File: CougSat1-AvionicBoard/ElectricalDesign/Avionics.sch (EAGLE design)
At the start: 195 parts, among them J11 -Y, J12 +Z, J13 +X, J14 -Z, J15 +Y, J3 SWD, J4 CougSat Card, J5 -X, J8 SWD, J9 SWD, U1 STM32L476RGT, U10 BNO055, U11 128KB, U12 TXS0102DQM, U13 TXS0102DQM, U14 AD8515, U15 BNO055, U16 BNO055, U17 TXS0102DQM, U18 TXS0102DQM, U19 INA199C1, U2 STM32L476RGT, U20 INA199C1, U21 INA199C1, U24 AD8515, U25 AD7291, U26 AD7291, U29 AD8515, U3 STM32L476RGT, U4 128KB, U5 DRV8837, U6 DRV8837, U7 DRV8837, U8 AD7291, U9 Venus838FLPx-L, Y1 16MHz ±10ppm, Y10 16MHz ±10ppm, Y2 32.768kHz ±10ppm, Y3 16MHz ±10ppm, Y4 32.768kHz ±10ppm, Y6 32.768kHz ±10ppm, Y7 32.768kHz ±10ppm, Y8 32.768kHz ±10ppm, Y9 32.768kHz ±10ppm

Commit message: Resolved Errors
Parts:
- J10: value (none) -> iFJR SD1
- J16: value (none) -> IFJR SD0
- J2: value (none) -> IHU SD1
- J6: value (none) -> IHU SD0
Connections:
- new net RFGND: AE1.SHIELD, R4.1, U9BASE.RFGND
- net 3.3V_0: now also C25.1, C26.1
- net AGND: no longer AE1.SHIELD, R4.1, U9BASE.RFGND
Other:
- note removed: "3D3>"
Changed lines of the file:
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@@
 <part name="SUPPLY3" library="CougsInSpace-PowerSymbols" deviceset="AGND" device=""/>
 <part name="SUPPLY4" library="CougsInSpace-PowerSymbols" deviceset="CHASSIS" device=""/>
-<part name="SUPPLY5" library="CougsInSpace-PowerSymbols" deviceset="RFGND" device=""/>
 <part name="SUPPLY6" library="CougsInSpace-PowerSymbols" deviceset="DGND" device=""/>
 <part name="SUPPLY7" library="CougsInSpace-PowerSymbols" deviceset="DGND" device=""/>
@@
 <part name="R12" library="CougsInSpace-Resistors" deviceset="RES-V" device="-1608" technology="-33K" value="33kΩ 1%"/>
 <part name="SUPPLY56" library="CougsInSpace-PowerSymbols" deviceset="DGND" device=""/>
-<part name="SUPPLY57" library="CougsInSpace-PowerSymbols" deviceset="RFGND" device=""/>
 <part name="R13" library="CougsInSpace-Resistors" deviceset="RES-H" device="-1608" technology="-1K" value="1kΩ 0.1%"/>
 <part name="DS1" library="CougsInSpace-LEDs" deviceset="LED-V" device="-1608" technology="-GRN" value="Green"/>
@@
 <part name="OFFSHEET167" library="CougsInSpace-Aesthetics" deviceset="OFF_SHEET-OUT" device=""/>
 <part name="OFFSHEET168" library="CougsInSpace-Aesthetics" deviceset="OFF_SHEET-IN" device=""/>
-<part name="J10" library="CougsInSpace-Connectors" deviceset="µSD-SW" device="-PUSH-PUSH"/>
-<part name="J16" library="CougsInSpace-Connectors" deviceset="µSD-SW" device="-PUSH-PUSH"/>
+<part name="J10" library="CougsInSpace-Connectors" deviceset="µSD-SW" device="-PUSH-PUSH" value="iFJR SD1"/>
+<part name="J16" library="CougsInSpace-Connectors" deviceset="µSD-SW" device="-PUSH-PUSH" value="IFJR SD0"/>
 <part name="SUPPLY115" library="CougsInSpace-PowerSymbols" deviceset="DGND" device=""/>
 <part name="SUPPLY116" library="CougsInSpace-PowerSymbols" deviceset="DGND" device=""/>
@@
 <part name="C33" library="CougsInSpace-Capacitors" deviceset="CAP-V" device="-3216" technology="-100NF" value="100nF 10%"/>
 <part name="C35" library="CougsInSpace-Capacitors" deviceset="CAP-V" device="-1608" technology="-6.8NF" value="6.8nF 5%"/>
-<part name="J2" library="CougsInSpace-Connectors" deviceset="µSD-SW" device="-PUSH-PUSH"/>
-<part name="J6" library="CougsInSpace-Connectors" deviceset="µSD-SW" device="-PUSH-PUSH"/>
+<part name="J2" library="CougsInSpace-Connectors" deviceset="µSD-SW" device="-PUSH-PUSH" value="IHU SD1"/>
+<part name="J6" library="CougsInSpace-Connectors" deviceset="µSD-SW" device="-PUSH-PUSH" value="IHU SD0"/>
 <part name="SUPPLY75" library="CougsInSpace-PowerSymbols" deviceset="DGND" device=""/>
 <part name="SUPPLY76" library="CougsInSpace-PowerSymbols" deviceset="DGND" device=""/>
@@
 <part name="SUPPLY79" library="CougsInSpace-PowerSymbols" deviceset="3.3V-0" device=""/>
 <part name="SUPPLY81" library="CougsInSpace-PowerSymbols" deviceset="3.3V-0" device=""/>
+<part name="SUPPLY91" library="CougsInSpace-PowerSymbols" deviceset="3.3V-0" device=""/>
+<part name="SUPPLY92" library="CougsInSpace-PowerSymbols" deviceset="3.3V-0" device=""/>
+<part name="SUPPLY5" library="CougsInSpace-PowerSymbols" deviceset="RFGND" device=""/>
+<part name="SUPPLY57" library="CougsInSpace-PowerSymbols" deviceset="RFGND" device=""/>
 </parts>
 <sheets>
@@
 <instance part="SUPPLY3" gate="G$1" x="30.48" y="10.16" smashed="yes"/>
 <instance part="SUPPLY4" gate="G$1" x="45.72" y="10.16" smashed="yes"/>
-<instance part="SUPPLY5" gate="G$1" x="60.96" y="10.16" smashed="yes"/>
 <instance part="DIA23" gate="G$1" x="172.72" y="121.92" smashed="yes"/>
 <instance part="DIA24" gate="G$1" x="205.74" y="121.92" smashed="yes"/>
+<instance part="SUPPLY5" gate="G$1" x="60.96" y="10.16" smashed="yes"/>
 </instances>
 <busses>
@@
 <wire x1="30.48" y1="15.24" x2="30.48" y2="12.7" width="0.1524" layer="91"/>
 </segment>
-<segment>
-<pinref part="R4" gate="G$1" pin="1"/>
-<pinref part="SUPPLY5" gate="G$1" pin="RFGND"/>
-<wire x1="60.96" y1="15.24" x2="60.96" y2="12.7" width="0.1524" layer="91"/>
-</segment>
 </net>
 <net name="CHASSIS" class="0">
@@
 </segment>
 </net>
+<net name="RFGND" class="0">
+<segment>
+<pinref part="R4" gate="G$1" pin="1"/>
+<pinref part="SUPPLY5" gate="G$1" pin="RFGND"/>
+<wire x1="60.96" y1="15.24" x2="60.96" y2="12.7" width="0.1524" layer="91"/>
+</segment>
+</net>
 </nets>
 </sheet>
@@
 <text x="200.66" y="127" size="1.27" layer="97" align="center-left"> &lt;9B6</text>
 <text x="48.26" y="124.46" size="1.27" layer="97" align="center-left">   3D5&gt;</text>
-<text x="144.78" y="127" size="1.27" layer="97" align="center-left">   3D3&gt;</text>
 <text x="200.66" y="40.64" size="1.27" layer="97" align="center-right">3B2&gt; </text>
 <wire x1="91.44" y1="60.96" x2="91.44" y2="33.02" width="0.1524" layer="97" style="shortdash"/>
@@
 </instance>
 <instance part="SUPPLY56" gate="1" x="73.66" y="86.36" smashed="yes"/>
-<instance part="SUPPLY57" gate="G$1" x="114.3" y="114.3" smashed="yes"/>
 <instance part="R13" gate="G$1" x="132.08" y="99.06" smashed="yes">
 <attribute name="NAME" x="130.81" y="101.092" size="1.27" layer="95" align="center"/>
@@
 <attribute name="VALUE" x="60.96" y="77.216" size="1.27" layer="96" align="center"/>
 </instance>
+<instance part="SUPPLY57" gate="G$1" x="116.84" y="114.3" smashed="yes"/>
 </instances>
 <busses>
@@
 <net name="AGND" class="0">
 <segment>
-<pinref part="U9" gate="BASE" pin="RFGND"/>
-<wire x1="101.6" y1="116.84" x2="114.3" y2="116.84" width="0.1524" layer="91"/>
-<pinref part="SUPPLY57" gate="G$1" pin="RFGND"/>
-<wire x1="114.3" y1="116.84" x2="124.46" y2="116.84" width="0.1524" layer="91"/>
-<junction x="114.3" y="116.84"/>
-<pinref part="AE1" gate="G$1" pin="SHIELD"/>
-</segment>
-<segment>
 <pinref part="RT1" gate="G$1" pin="1"/>
 <pinref part="SUPPLY97" gate="G$1" pin="AGND"/>
@@
 </segment>
 </net>
+<net name="RFGND" class="0">
+<segment>
+<pinref part="U9" gate="BASE" pin="RFGND"/>
+<wire x1="101.6" y1="116.84" x2="116.84" y2="116.84" width="0.1524" layer="91"/>
+<pinref part="AE1" gate="G$1" pin="SHIELD"/>
+<pinref part="SUPPLY57" gate="G$1" pin="RFGND"/>
+<wire x1="116.84" y1="116.84" x2="124.46" y2="116.84" width="0.1524" layer="91"/>
+<junction x="116.84" y="116.84"/>
+</segment>
+</net>
 </nets>
 </sheet>
@@
 <attribute name="VALUE" x="40.64" y="135.636" size="1.27" layer="96" align="center"/>
 </instance>
+<instance part="SUPPLY91" gate="G$1" x="111.76" y="160.02" smashed="yes">
+<attribute name="VALUE" x="111.76" y="163.576" size="1.27" layer="96" align="center"/>
+</instance>
+<instance part="SUPPLY92" gate="G$1" x="111.76" y="119.38" smashed="yes">
+<attribute name="VALUE" x="111.76" y="122.936" size="1.27" layer="96" align="center"/>
+</instance>
 </instances>
 <busses>
@@
 </segment>
 </net>
-<net name="3.3V_6" class="0">
-<segment>
-<pinref part="C65" gate="G$1" pin="1"/>
-<pinref part="SUPPLY221" gate="G$1" pin="3.3V_6"/>
-</segment>
-</net>
 <net name="AGND" class="0">
 <segment>
@@
 <pinref part="SUPPLY81" gate="G$1" pin="3.3V_0"/>
 </segment>
+<segment>
+<pinref part="C25" gate="G$1" pin="1"/>
+<pinref part="SUPPLY91" gate="G$1" pin="3.3V_0"/>
+</segment>
+<segment>
+<pinref part="C26" gate="G$1" pin="1"/>
+<pinref part="SUPPLY92" gate="G$1" pin="3.3V_0"/>
+</segment>
 </net>
 <net name="AVREF-1" class="0">
@@
 </segment>
 </net>
+<net name="3.3V_6" class="0">
+<segment>
+<pinref part="C65" gate="G$1" pin="1"/>
+<pinref part="SUPPLY221" gate="G$1" pin="3.3V_6"/>
+</segment>
+</net>
 </nets>
 </sheet>
@@
 <net name="COIL-Y_COIL-" class="0">
 <segment>
-<wire x1="78.74" y1="165.1" x2="99.06" y2="165.1" width="0.1524" layer="91"/>
-<wire x1="99.06" y1="165.1" x2="101.6" y2="165.1" width="0.1524" layer="91"/>
+<wire x1="78.74" y1="165.1" x2="101.6" y2="165.1" width="0.1524" layer="91"/>
 <pinref part="J11" gate="G$1" pin="4"/>
 <label x="81.28" y="165.1" size="1.778" layer="95"/>
@@
 <net name="COIL-Z_+" class="0">
 <segment>
-<wire x1="144.78" y1="167.64" x2="165.1" y2="167.64" width="0.1524" layer="91"/>
-<wire x1="165.1" y1="167.64" x2="167.64" y2="167.64" width="0.1524" layer="91"/>
+<wire x1="144.78" y1="167.64" x2="167.64" y2="167.64" width="0.1524" layer="91"/>
 <pinref part="J12" gate="G$1" pin="3"/>
 <label x="147.32" y="167.64" size="1.778" layer="95"/>
@@
 <net name="COIL-Z_COIL-" class="0">
 <segment>
-<wire x1="144.78" y1="165.1" x2="165.1" y2="165.1" width="0.1524" layer="91"/>
-<wire x1="165.1" y1="165.1" x2="167.64" y2="165.1" width="0.1524" layer="91"/>
+<wire x1="144.78" y1="165.1" x2="167.64" y2="165.1" width="0.1524" layer="91"/>
 <pinref part="J12" gate="G$1" pin="4"/>
 <label x="147.32" y="165.1" size="1.778" layer="95"/>
@@
 </segment>
 <segment>
-<wire x1="78.74" y1="172.72" x2="99.06" y2="172.72" width="0.1524" layer="91"/>
+<wire x1="78.74" y1="172.72" x2="101.6" y2="172.72" width="0.1524" layer="91"/>
 <label x="81.28" y="172.72" size="1.778" layer="95"/>
-<wire x1="99.06" y1="172.72" x2="101.6" y2="172.72" width="0.1524" layer="91"/>
 <pinref part="J11" gate="G$1" pin="1"/>
 </segment>
@@
 </segment>
 <segment>
-<wire x1="144.78" y1="170.18" x2="165.1" y2="170.18" width="0.1524" layer="91"/>
+<wire x1="144.78" y1="170.18" x2="167.64" y2="170.18" width="0.1524" layer="91"/>
 <label x="147.32" y="170.18" size="1.778" layer="95"/>
-<wire x1="165.1" y1="170.18" x2="167.64" y2="170.18" width="0.1524" layer="91"/>
 <pinref part="J12" gate="G$1" pin="2"/>
 </segment>
@@
 </sheet>
 </sheets>
+<errors>
+</errors>
 </schematic>
 </drawing>

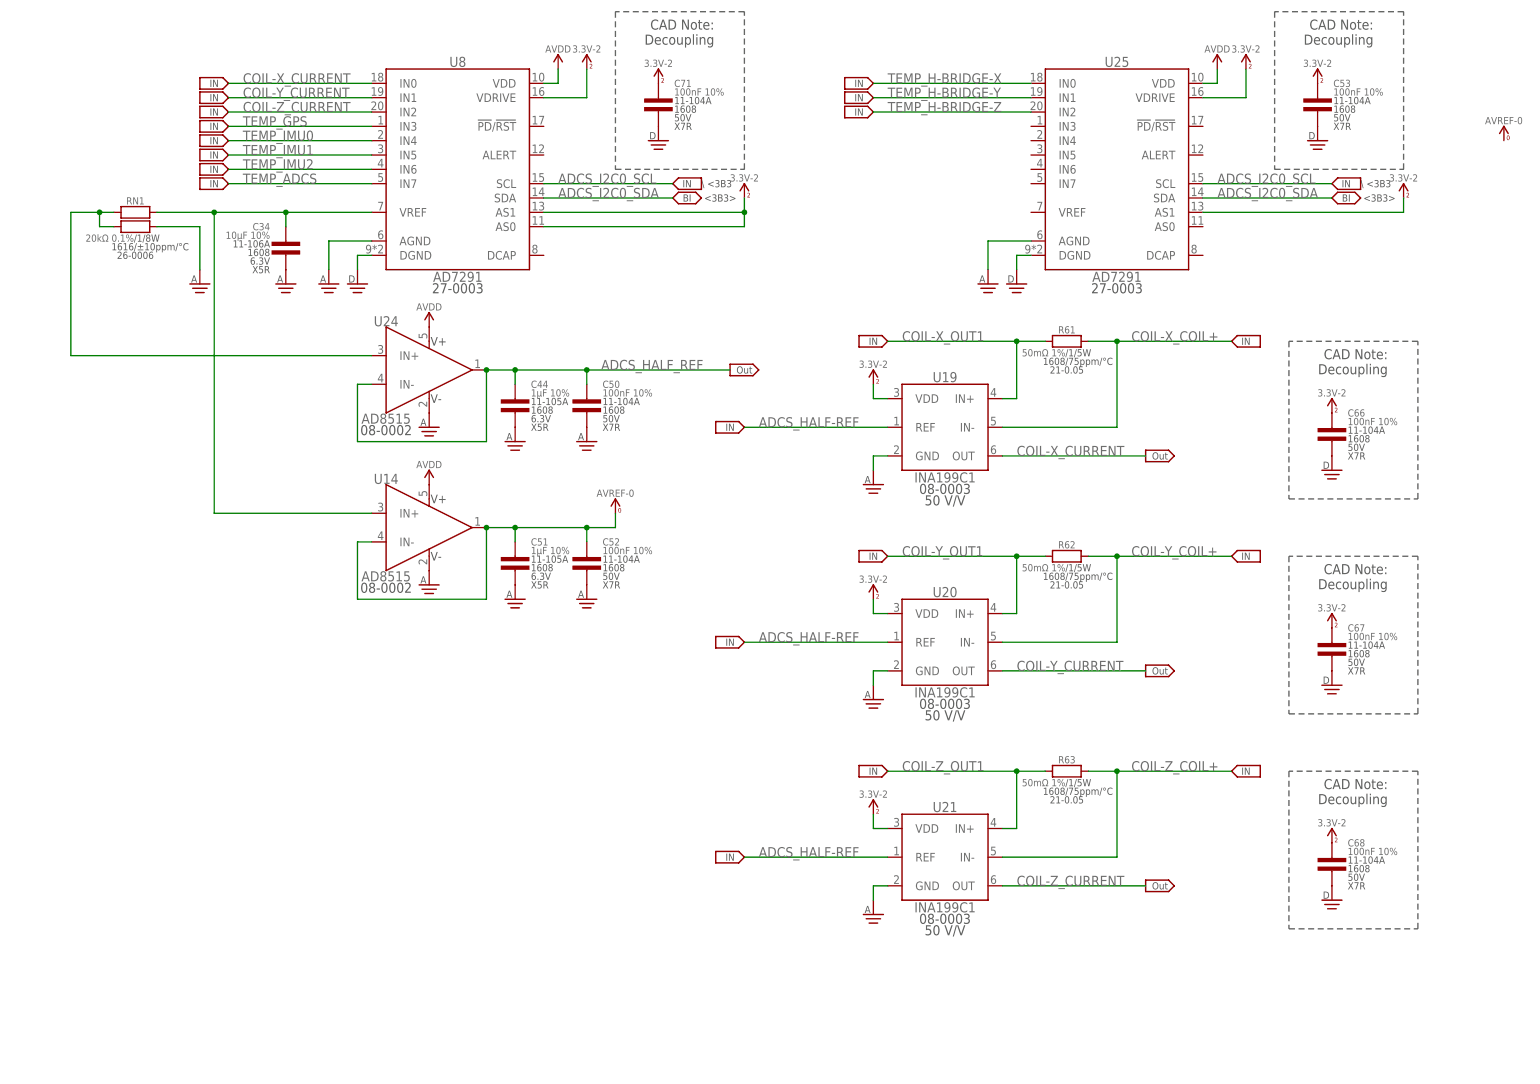
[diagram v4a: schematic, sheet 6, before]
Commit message: Updated Off-sheet Connectors
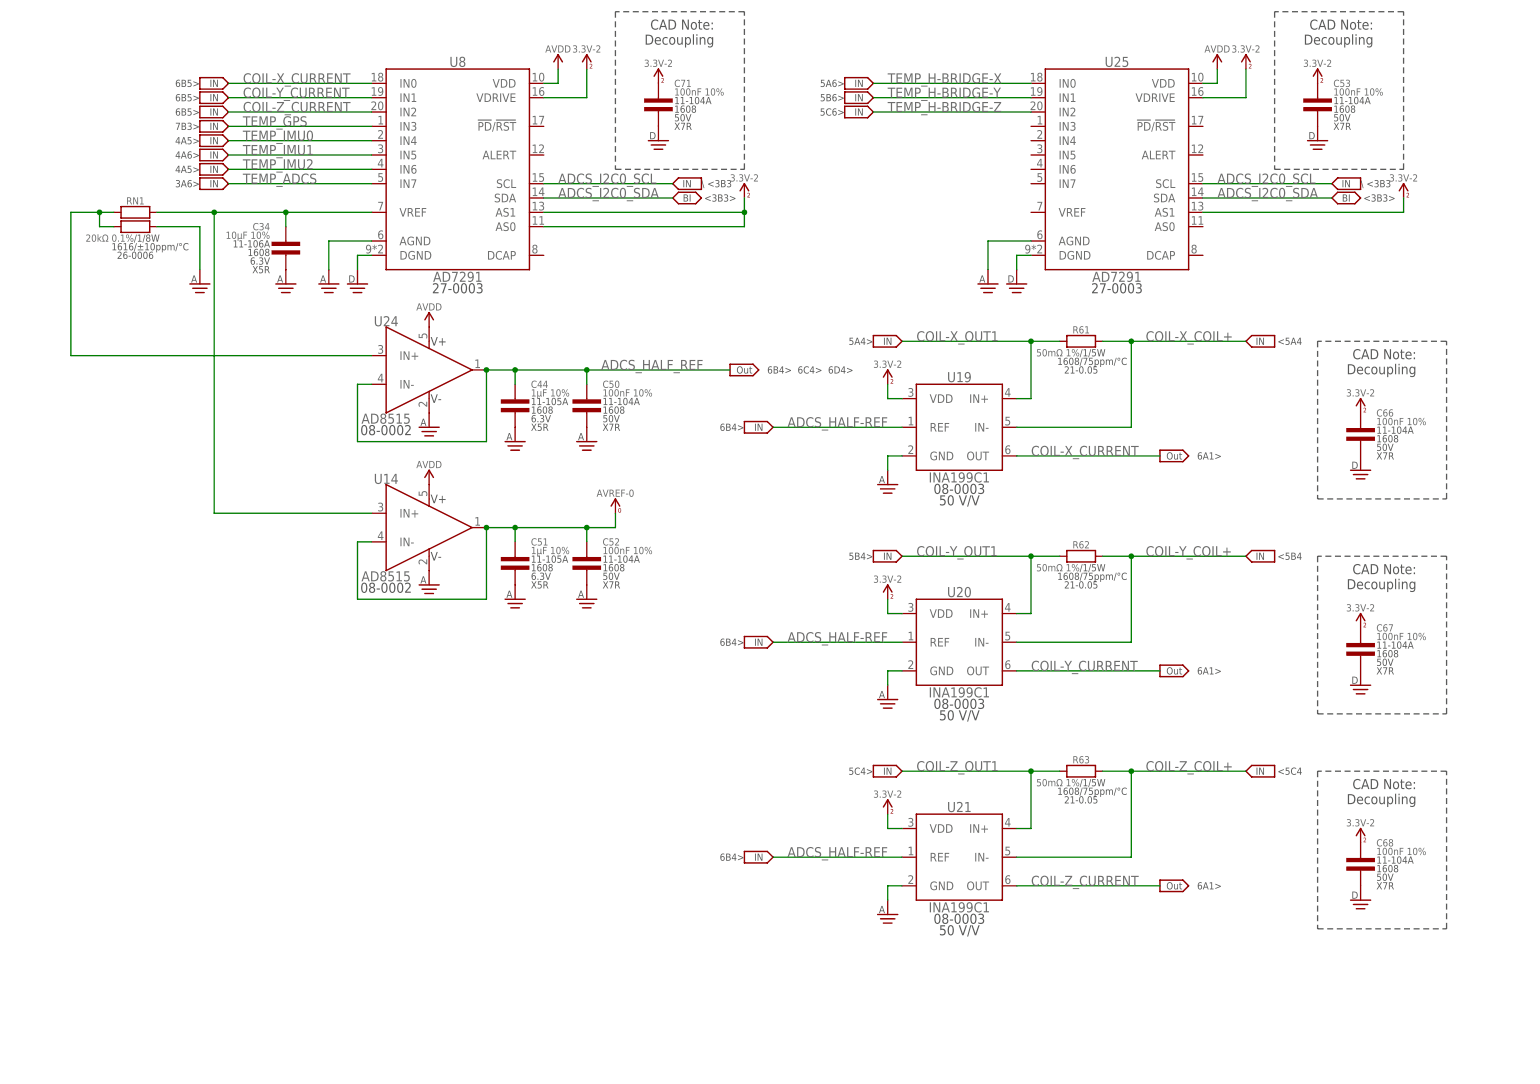
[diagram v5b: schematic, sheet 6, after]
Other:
- note added: "10C1>"
- note added: "3D2> 3D2> 4A3> 4C3> 6A3> 6A6>"
- note added: "4A5>"
- note added: "4A6>"
- note added: "5A4>"
- note added: "5A6>"
- note added: "5B4>"
- note added: "5B6>"
- note added: "5C4>"
- note added: "5C6>"
- note added: "6B4>"
- note added: "6B4> 6C4> 6D4>"
- note added: "6B5>"
- note added: "6B6>"
- note added: "6C4>"
- note added: "6C6>"
- note added: "6D4>"
- note added: "6D6>"
- note added: "7B3>"
- note added: "8D4>"
- note added: "8D5>"
- note added: "9A1>"
- note added: "9B6> 10C3>"
- note added: "<3D2><3D2><4A3><4C3><6A3><6A6>"
- note added: "<5A4"
- note added: "<5B4"
- note added: "<5C4"
- note added: "<9B6><10C3>"
- note added: "Page 10: IHU Cards & C&DH ADC Page 11: Power & ADCS Jacks"
- note added: "Page 1: Block Diagram Page 2: Power Rails Page 3: ADCS Page 4: IMUs Page 5: H-Bridges Page 6: ADCS ADCs & Amplifiers Page 7: GPS Page 8: IFJR Page 9: C&DH"
- note removed: "3C2> 3D2> 4A3> 4C3> 6B4>"
- note removed: "6A2>"
- note removed: "<3C2><3D2><4A3><4C3><6B4>"
- note removed: "Page 10: Power & ADCS Jacks"
- note removed: "Page 1: Block Diagram Page 2: Power Rails Page 3: ADCS Page 4: IMUs Page 5: H-Bridges Page 6: ADCs Page 7: GPS Page 8: IFJR Page 9: C&DH"
- moved on the sheet: C13, C14, C66, C67, C68, R19, R21, R22, R26, R59, R60, R61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
